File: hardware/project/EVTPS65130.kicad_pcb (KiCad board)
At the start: 2 copper layers, 52 parts, among them J2 Conn_01x04_Pin, Q10 PMOS, U3 TPS65130RGE

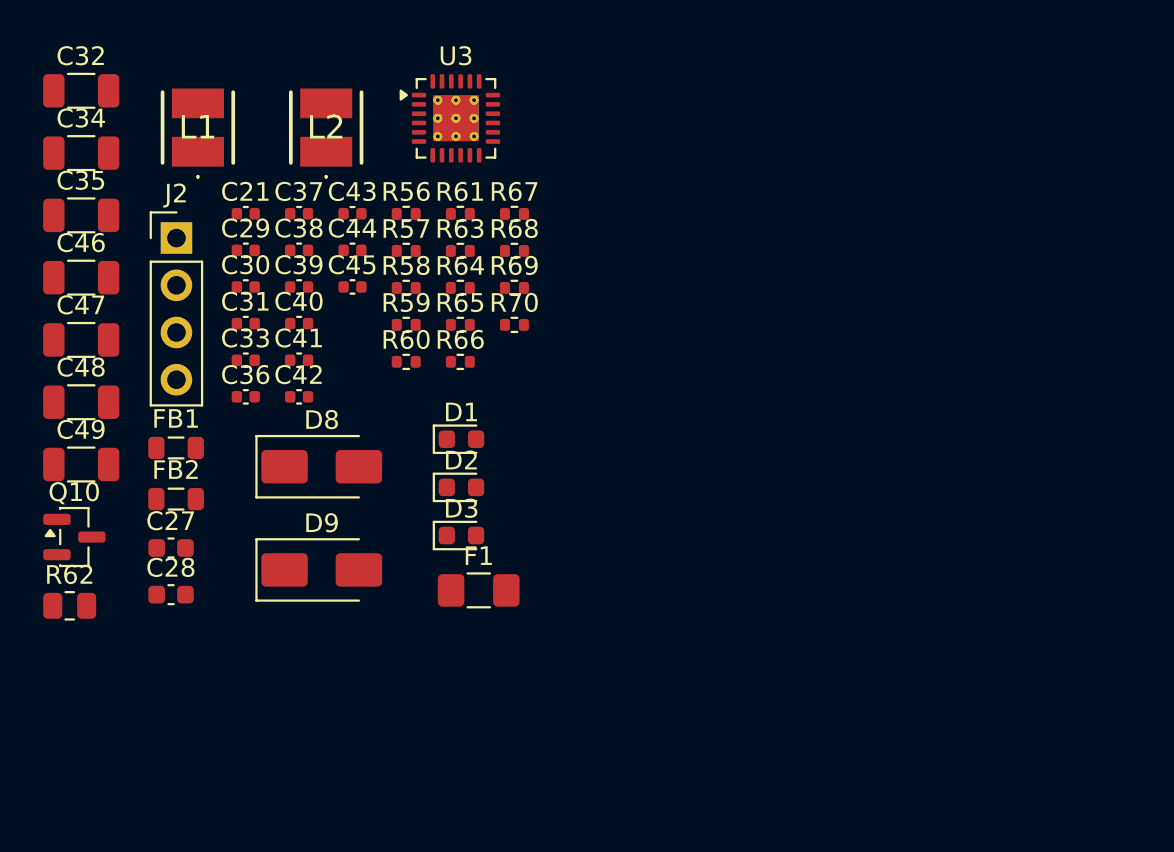
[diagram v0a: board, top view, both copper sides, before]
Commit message: Started PCB placement
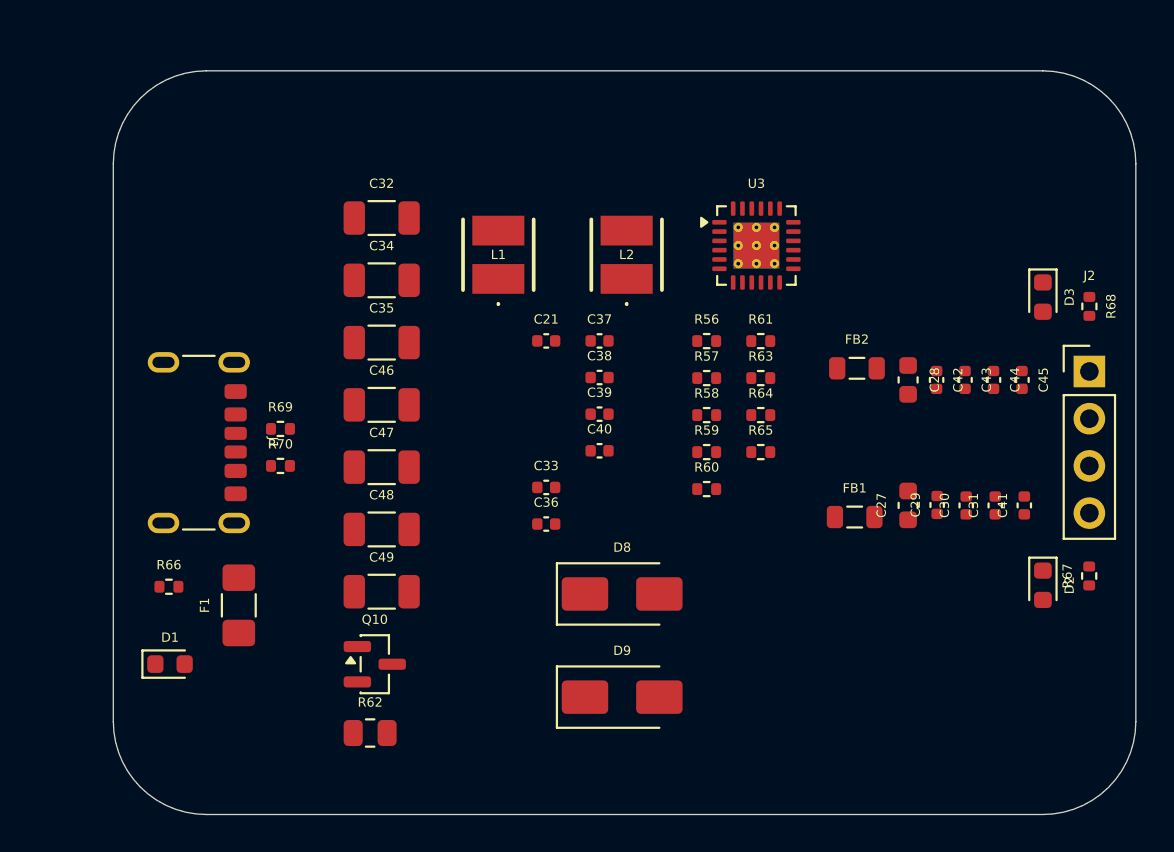
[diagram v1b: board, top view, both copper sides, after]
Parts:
- added J1: USB_C_Receptacle_PowerOnly_6P, Connector_USB:USB_C_Receptacle_GCT_USB4125-xx-x-0190_6P_TopMnt_Horizontal, F.Cu at (126.0, 100.0)
- moved J2 49.6 mm to (175.0, 96.2)
- moved C31 41.5 mm to (169.9, 103.4), turned to 90 degrees
- moved C28 41.3 mm to (165.2, 96.6), turned to -90 degrees
- moved C30 40.5 mm to (168.4, 103.4), turned to 90 degrees
- moved C41 39.8 mm to (171.5, 103.4), turned to 90 degrees
- moved C27 39.7 mm to (165.2, 103.4), turned to 90 degrees
- moved C29 39.6 mm to (166.8, 103.3), turned to 90 degrees
- moved FB2 37.3 mm to (162.5, 96.0)
- moved FB1 36.7 mm to (162.4, 104.0)
- moved R67 36.5 mm to (175.0, 107.2), turned to 90 degrees
- moved C45 36.4 mm to (171.4, 96.6), turned to -90 degrees
- moved C44 35.2 mm to (169.8, 96.6), turned to -90 degrees
- moved C42 34.3 mm to (166.8, 96.6), turned to -90 degrees
- moved C43 34.1 mm to (168.3, 96.6), turned to -90 degrees
- moved D3 33.8 mm to (172.5, 92.2), turned to -90 degrees
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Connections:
- C27 pad 2: AGND -> GND
- C28 pad 2: AGND -> GND
- C29 pad 2: AGND -> GND
- C30 pad 2: AGND -> GND
- C31 pad 2: AGND -> GND
- C32 pad 2: AGND -> GND
- C33 pad 2: AGND -> GND
- C34 pad 2: AGND -> GND
- C35 pad 2: AGND -> GND
- C41 pad 2: AGND -> GND
- C42 pad 2: AGND -> GND
- C43 pad 2: AGND -> GND
- C44 pad 2: AGND -> GND
- C45 pad 2: AGND -> GND
- C46 pad 2: AGND -> GND
- C47 pad 2: AGND -> GND
- C48 pad 2: AGND -> GND
- C49 pad 2: AGND -> GND
- D1 pad 1: AGND -> GND
- D2 pad 1: AGND -> GND
- D3 pad 2: AGND -> GND
- J2 pad 2: AGND -> GND
- J2 pad 3: AGND -> GND
- L2 pad 1: AGND -> GND
- R69 pad 2: AGND -> GND
- R70 pad 1: AGND -> GND
- U3 pad 2: AGND -> GND
- U3 pad 25: AGND -> GND
- U3 pad 3: AGND -> GND
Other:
- board outline added: 55 x 40 mm
